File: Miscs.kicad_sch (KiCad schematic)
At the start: 18 parts, among them J8 MEM2080-00-128-00-A_REVA, Q2 SI7232DN-T1-GE3, U11 XTSD08GLGEAG

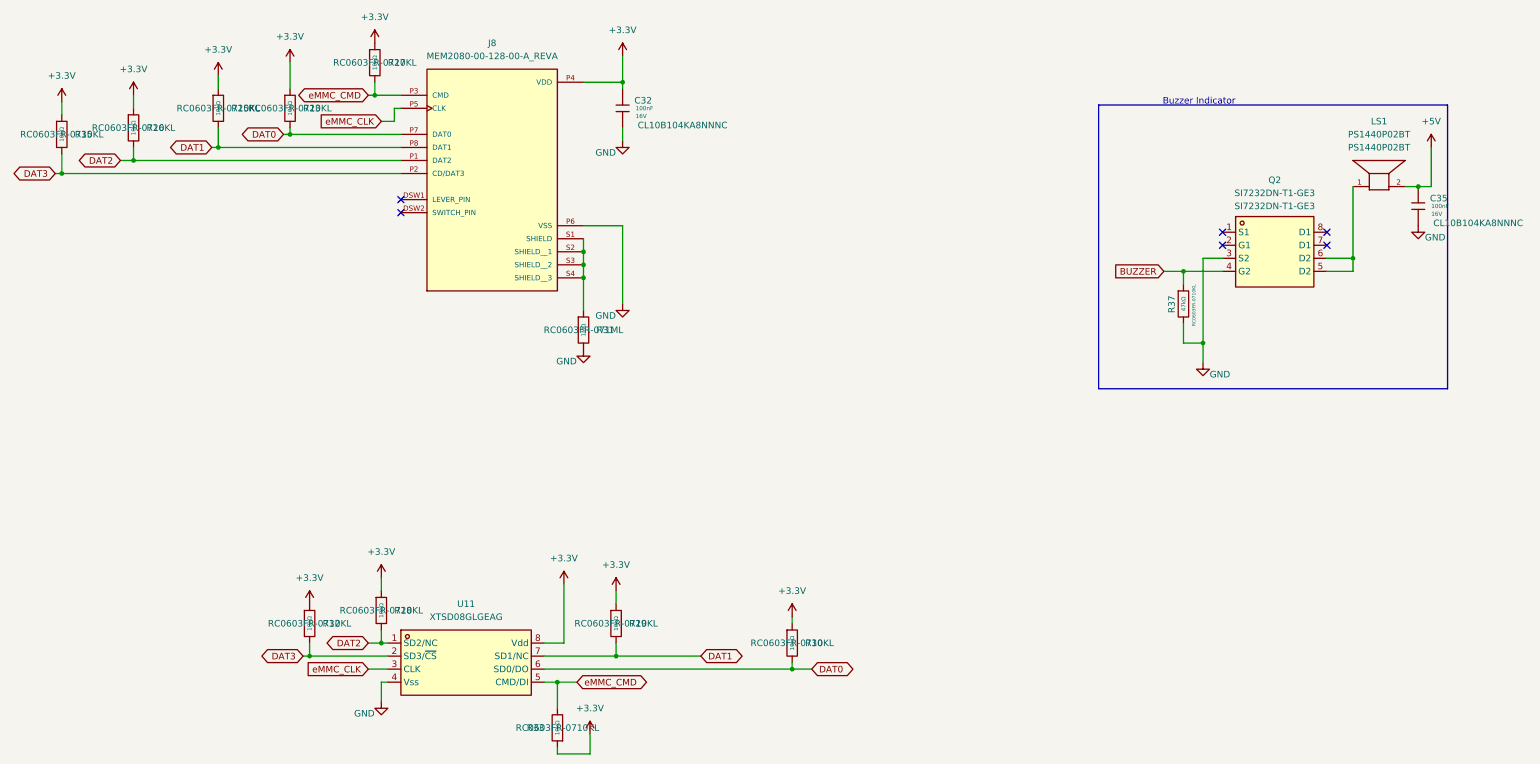
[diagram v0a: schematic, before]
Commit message: fixes
Fixed mmc, power
Added external 5V Supply
Added external reset button
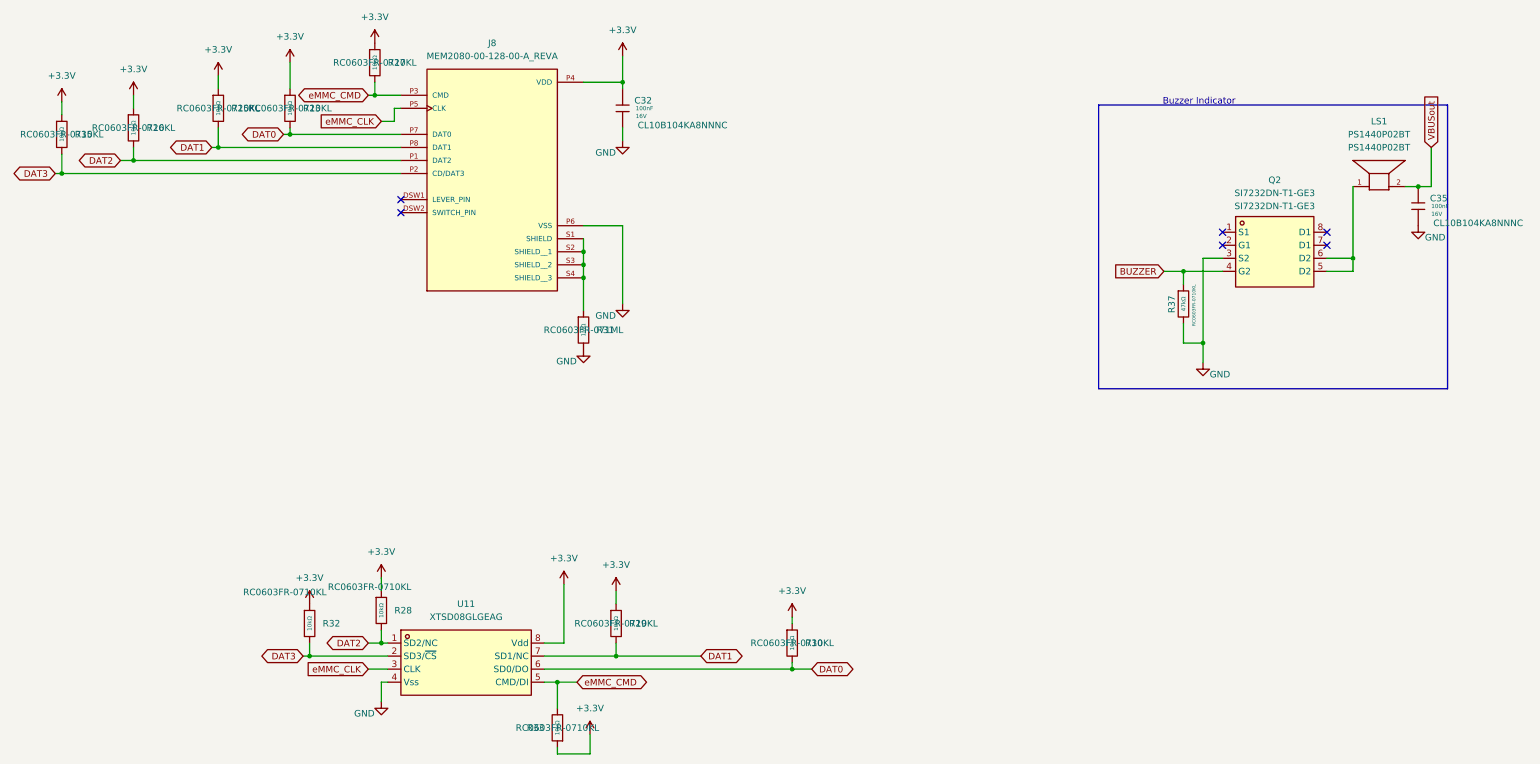
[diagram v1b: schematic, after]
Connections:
- net +5V renamed VBUSout
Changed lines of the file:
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@@
 		)
 	)
+	(global_label "VBUSout"
+		(shape input)
+		(at 297.18 88.9 90)
+		(fields_autoplaced yes)
+		(effects
+			(font
+				(size 1.27 1.27)
+			)
+			(justify left)
+		)
+		(property "Intersheetrefs" "${INTERSHEET_REFS}"
+			(at 297.18 77.9925 90)
+			(effects
+				(font
+					(size 1.27 1.27)
+				)
+				(justify left)
+				(hide yes)
+			)
+		)
+	)
 	(global_label "DAT2"
 		(shape bidirectional)
@@
 		(on_board no)
 		(dnp no)
-		(fields_autoplaced yes)
 		(property "Reference" "R28"
 			(at 95.25 179.0699 0)
@@
 		)
 		(property "Digikey Parts" " RC0603FR-0710KL"
-			(at 92.71 179.07 0)
+			(at 90.424 174.498 0)
 			(effects
 				(font
@@
 	)
 	(symbol
-		(lib_id "power:+5V")
-		(at 297.18 88.9 0)
-		(unit 1)
-		(exclude_from_sim no)
-		(in_bom yes)
-		(on_board yes)
-		(dnp no)
-		(fields_autoplaced yes)
-		(property "Reference" "#PWR054"
-			(at 297.18 92.71 0)
-			(effects
-				(font
-					(size 1.27 1.27)
-				)
-				(hide yes)
-			)
-		)
-		(property "Value" "+5V"
-			(at 297.18 83.82 0)
-			(effects
-				(font
-					(size 1.27 1.27)
-				)
-			)
-		)
-		(property "Footprint" ""
-			(at 297.18 88.9 0)
-			(effects
-				(font
-					(size 1.27 1.27)
-				)
-				(hide yes)
-			)
-		)
-		(property "Datasheet" ""
-			(at 297.18 88.9 0)
-			(effects
-				(font
-					(size 1.27 1.27)
-				)
-				(hide yes)
-			)
-		)
-		(property "Description" "Power symbol creates a global label with name \"+5V\""
-			(at 297.18 88.9 0)
-			(effects
-				(font
-					(size 1.27 1.27)
-				)
-				(hide yes)
-			)
-		)
-		(pin "1"
-		)
-		(instances
-			(project ""
-				(path "/d402aac1-6798-4745-a2ce-fc3f8e4c9afb/e5fd5176-e33b-4137-b737-1b6a7c4448a9"
-					(reference "#PWR054")
-					(unit 1)
-				)
-			)
-		)
-	)
-	(symbol
 		(lib_id "power:+3.3V")
 		(at 133.35 203.2 0)
@@
 		(on_board no)
 		(dnp no)
-		(fields_autoplaced yes)
 		(property "Reference" "R32"
 			(at 81.28 181.6099 0)
@@
 		)
 		(property "Digikey Parts" " RC0603FR-0710KL"
-			(at 78.74 181.61 0)
+			(at 73.914 175.514 0)
 			(effects
 				(font
